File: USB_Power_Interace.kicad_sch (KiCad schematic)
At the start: 26 parts, among them CN1 USC_C_Receptacle_Hirose_CX90M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, SW1 SPST-NO, SW2 SPST-NO, U3 TPS2117DRL, U4 NCP167, U8 74HCT00

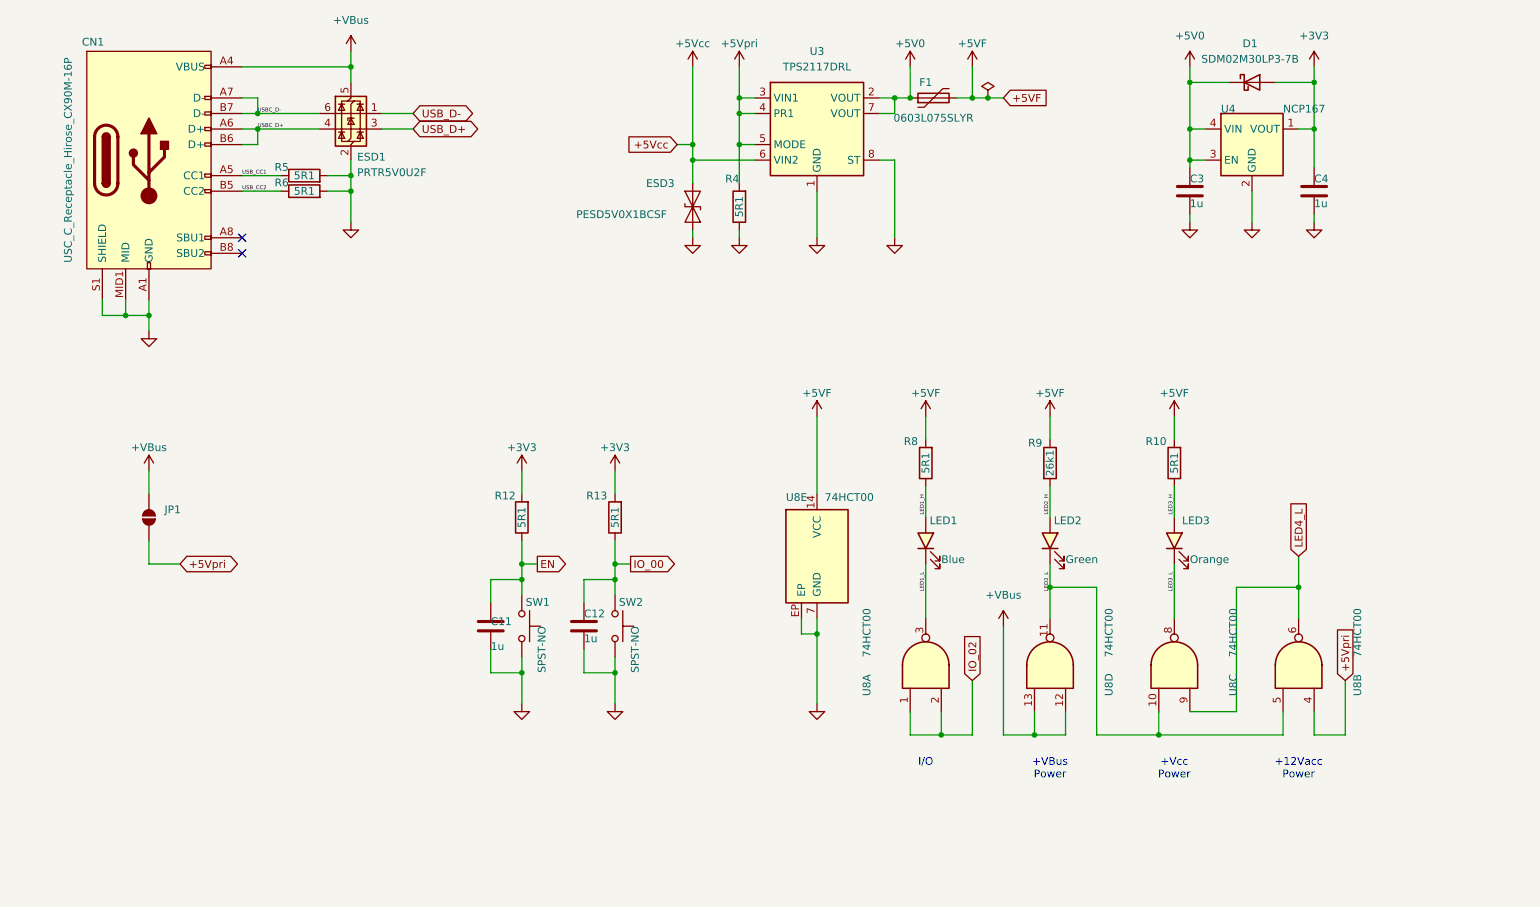
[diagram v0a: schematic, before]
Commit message: successful 1st pass, but I want to try some new bus'ing techniques to clean up the routing
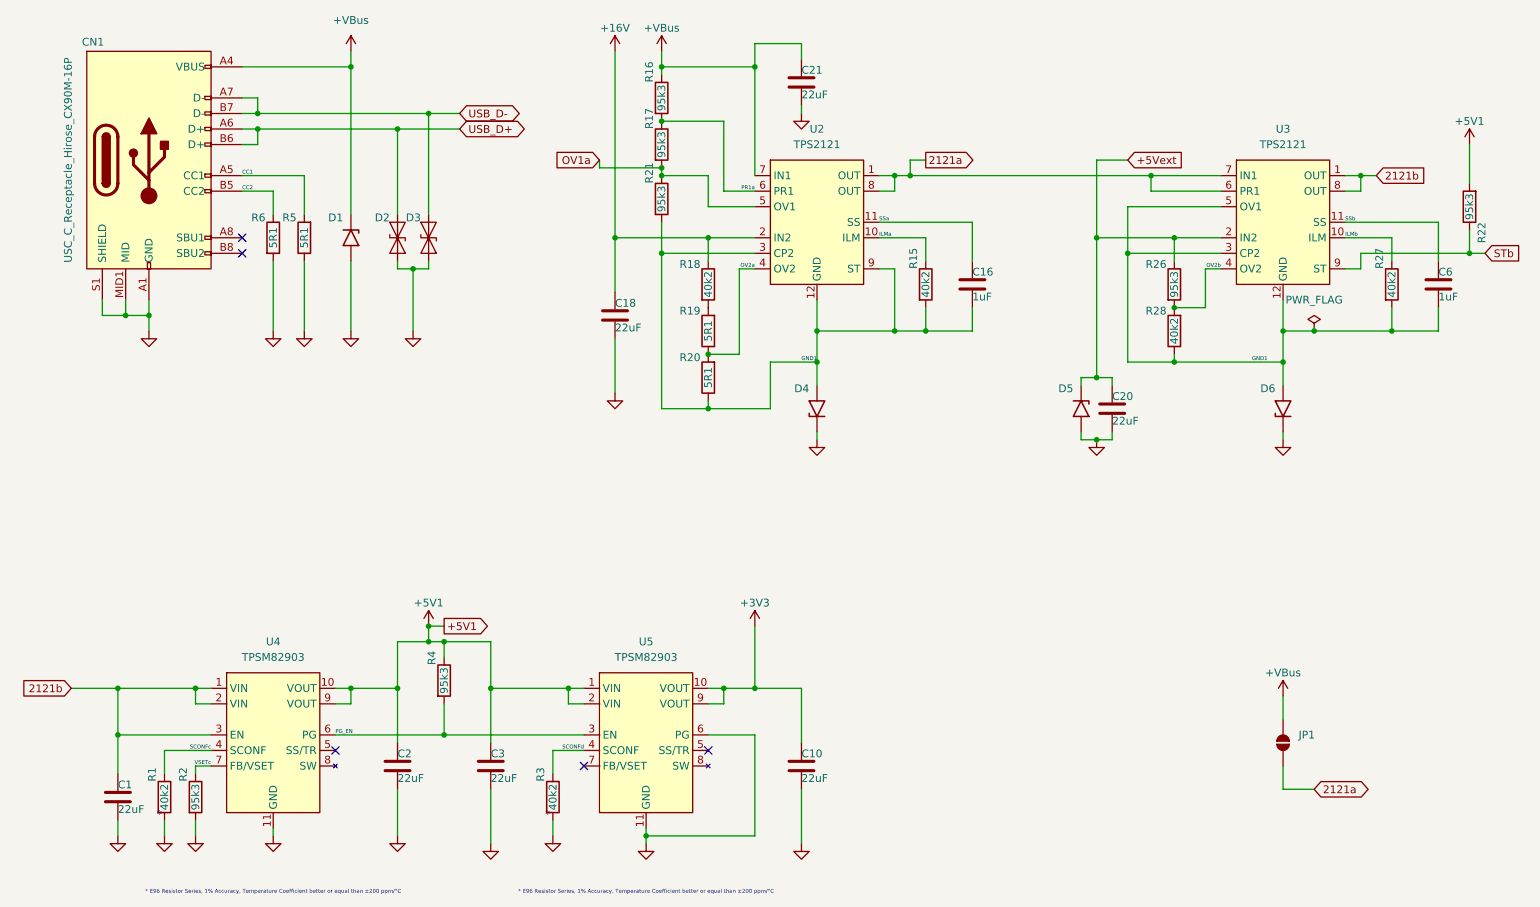
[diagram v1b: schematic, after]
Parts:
- removed C11, C12, C4: 1u, Capacitors:C0402_Nominal, symbol Device:C
- removed D1: SDM02M30LP3-7B, Personal_FootprintLibrary:DSN0603-2, symbol PersonalSchematicSymbolLibrary:SDM02M30LP3-7B
- removed ESD1: PRTR5V0U2F, Personal_FootprintLibrary:XSON6, symbol PersonalSchematicSymbolLibrary:PRTR5V0U2F
- removed ESD3: PESD5V0X1BCSF, Personal_FootprintLibrary:DSN0603-2, symbol PersonalSchematicSymbolLibrary:PESD5V0X1BCSF
- removed F1: 6V, 750mA, Personal_FootprintLibrary:Fuse_0603_1608Metric, symbol Device:Polyfuse
- removed LED1: Blue, Personal_FootprintLibrary:LED_0201-2, symbol PersonalSchematicSymbolLibrary:LED_Blue
- removed LED2: Green, Personal_FootprintLibrary:LED_0201-2, symbol PersonalSchematicSymbolLibrary:LED_Green
- removed LED3: Orange, Personal_FootprintLibrary:LED_0201-2, symbol PersonalSchematicSymbolLibrary:LED_Orange
- removed R10, R12, R13, R8: 5R1, Resistors:R0201_Nominal, symbol Device:R
- removed R9: 26k1, Resistors:R0201_Nominal, symbol Device:R
- removed SW1, SW2: SPST-NO, Personal_FootprintLibrary:SW_SPST_B3U_series, symbol PersonalSchematicSymbolLibrary:SW_Push_Button_NO
- removed U3: TPS2117DRL, Personal_FootprintLibrary:SOT5x3, symbol PersonalSchematicSymbolLibrary:TPS2117DRL
- removed U4: NCP167, Personal_FootprintLibrary:XDFN4_1.0x1.0mm, symbol PersonalSchematicSymbolLibrary:NCP167
- removed U8: 74HCT00, Personal_FootprintLibrary:WQFN-14-1EP_2.5x3mm_P0.5mm_EP1x1.5mm, symbol 74xx:74HCT00
- added C1, C18: 22uF, Capacitors:C0603_Dense, symbol Device:C
- added C10, C2: 22uF, Capacitors:C0402_Nominal, symbol Device:C
- added C16, C6: 1uF, Capacitors:C0201_Dense, symbol Device:C
- added C20, C21: 22uF, Capacitors:C0402_Dense, symbol Device:C
- added D1, D4, D5, D6: VESD16C1-HD1HG3-08, Personal_FootprintLibrary:DFN1006-2, symbol PersonalSchematicSymbolLibrary:TVS_Unidirectional
- added D2, D3: PESD24VF1BL-Q, Personal_FootprintLibrary:DFN1006-2, symbol PersonalSchematicSymbolLibrary:PESD24VF1BBL-Q
- added R1, R15, R18, R27, R28, R3: 40k2, Resistors:R0201_Dense, symbol Device:R
- added R16, R17, R2, R21, R22, R26: 95k3, Resistors:R0201_Dense, symbol Device:R
- added R19, R20: 5R1, Resistors:R0201_Dense, symbol Device:R
- added U2, U3: TPS2121, Personal_FootprintLibrary:VQHN-HR-12, symbol PersonalSchematicSymbolLibrary:TPS2121
- added U4, U5: TPSM82903, Personal_FootprintLibrary:uSIP-11_3.0x2.8_ThermalVias, symbol PersonalSchematicSymbolLibrary:TPSM82903
- C3: value 1u -> 22uF; Distributor Link 1 https://www.digikey.com/en/products/detail/samsung-electro-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 -> https://www.digikey.com/en/products/detail/murata-electroni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; Distributor Link 2 https://www.mouser.com/ProductDetail/Samsung-Electro-Mechan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 -> https://www.mouser.com/ProductDetail/Murata-Electronics/GRM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; LCSC C52923 -> C3845593; Manufacturer Samsung -> Murata Electronics; Manufacturer Part Number CL05A105KA5NQNC -> GRM158R61A226ME15D
- R4: value 5R1 -> 95k3; footprint Resistors:R0201_Nominal -> Resistors:R0201_Dense; Distributor Link 2 https://www.mouser.com/ProductDetail/Royalohm/PF01WMF5100TE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 -> https://www.mouser.com/ProductDetail/Royalohm/0201WMF9532TE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; LCSC C50670526 -> C423395; Manufacturer Part Number PF01WMF510KTEE -> 0201WMF9532TEE
- R5, R6: footprint Resistors:R0201_Nominal -> Resistors:R0201_Dense
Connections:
- net USBC_D+ is gone; now on net USB_D+: CN1.A6 (D+), CN1.B6 (D+)
- net USBC_D- is gone; now on net USB_D-: CN1.A7 (D-), CN1.B7 (D-)
- net +3V3: now also C10.1, U5.10 (VOUT), U5.9 (VOUT)
- net +VBus: now also C21.1, D1.1 (A1), R16.1, U2.7 (IN1)
- net GND: now also R5.1, C1.2, C10.2, C18.2, C2.2, C20.2, C21.2, D1.2 (A2), D2.1 (A1), D3.1 (A1), D4.1 (A1), D5.2 (A2), D6.1 (A1), R1.2, R2.2, R3.2, U4.11 (GND), U5.11 (GND), U5.6 (PG); no longer R4.1, R5.2
- net USB_D+: now also D2.2 (A2)
- net USB_D-: now also D3.2 (A2)
- net +5V0 renamed +5V1
- net +5V1: now also R4.1, C2.1, R22.2, U4.10 (VOUT), U4.9 (VOUT), U5.1 (VIN), U5.2 (VIN)
- net +5Vpri renamed 2121a
- net 2121a: now also U2.1 (OUT), U2.8 (OUT), U3.6 (PR1), U3.7 (IN1); no longer R4.2
- net USB_CC1 renamed CC1
- net CC1: now also R5.2; no longer R5.1
- net USB_CC2 renamed CC2
- new net: R18.2, R19.2
- new net +16V: C18.1, R18.1, U2.2 (IN2)
- new net +5Vext: C20.1, D5.1 (A1), R26.1, U3.2 (IN2)
- new net 2121b: C1.1, U3.1 (OUT), U3.8 (OUT), U4.1 (VIN), U4.2 (VIN), U4.3 (EN)
- new net GND1: C16.2, C6.2, D4.2 (A2), D6.2 (A2), R15.2, R20.1, R21.2, R27.2, R28.1, U2.12 (GND), U2.3 (CP2), U2.9 (ST), U3.12 (GND), U3.3 (CP2), U3.5 (OV1)
- new net ILMa: R15.1, U2.10 (ILM)
- new net ILMb: R27.1, U3.10 (ILM)
- new net OV1a: R17.2, R21.1, U2.5 (OV1)
- new net OV2a: R19.1, R20.2, U2.4 (OV2)
- new net OV2b: R26.2, R28.2, U3.4 (OV2)
- new net PG_EN: R4.2, U4.6 (PG), U5.3 (EN)
- new net PR1a: R16.2, R17.1, U2.6 (PR1)
- new net SCONFc: R1.1, U4.4 (SCONF)
- new net SCONFd: R3.1, U5.4 (SCONF)
- new net SSa: C16.1, U2.11 (SS)
- new net SSb: C6.1, U3.11 (SS)
- new net STb: R22.1, U3.9 (ST)
- new net VSETc: R2.1, U4.7 (FB/VSET)
- no-connect marks 2 -> 5
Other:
- note added: "*"
- note added: "* E96 Resistor Series, 1% Accuracy, Temperature Coefficient better or equal than ±200 ppm/°C"
- note removed: "+12Vacc Power"
- note removed: "+VBus Power"
- note removed: "+Vcc Power"
- note removed: "I/O"
- moved on the sheet: JP1, R5, R6

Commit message: Update CAN_Interface.kicad_sch, ESP32-S3 Pico D1.kicad_dru, ESP32-S3 Pico D1.kicad_pcb, and 5 more files reroute completed
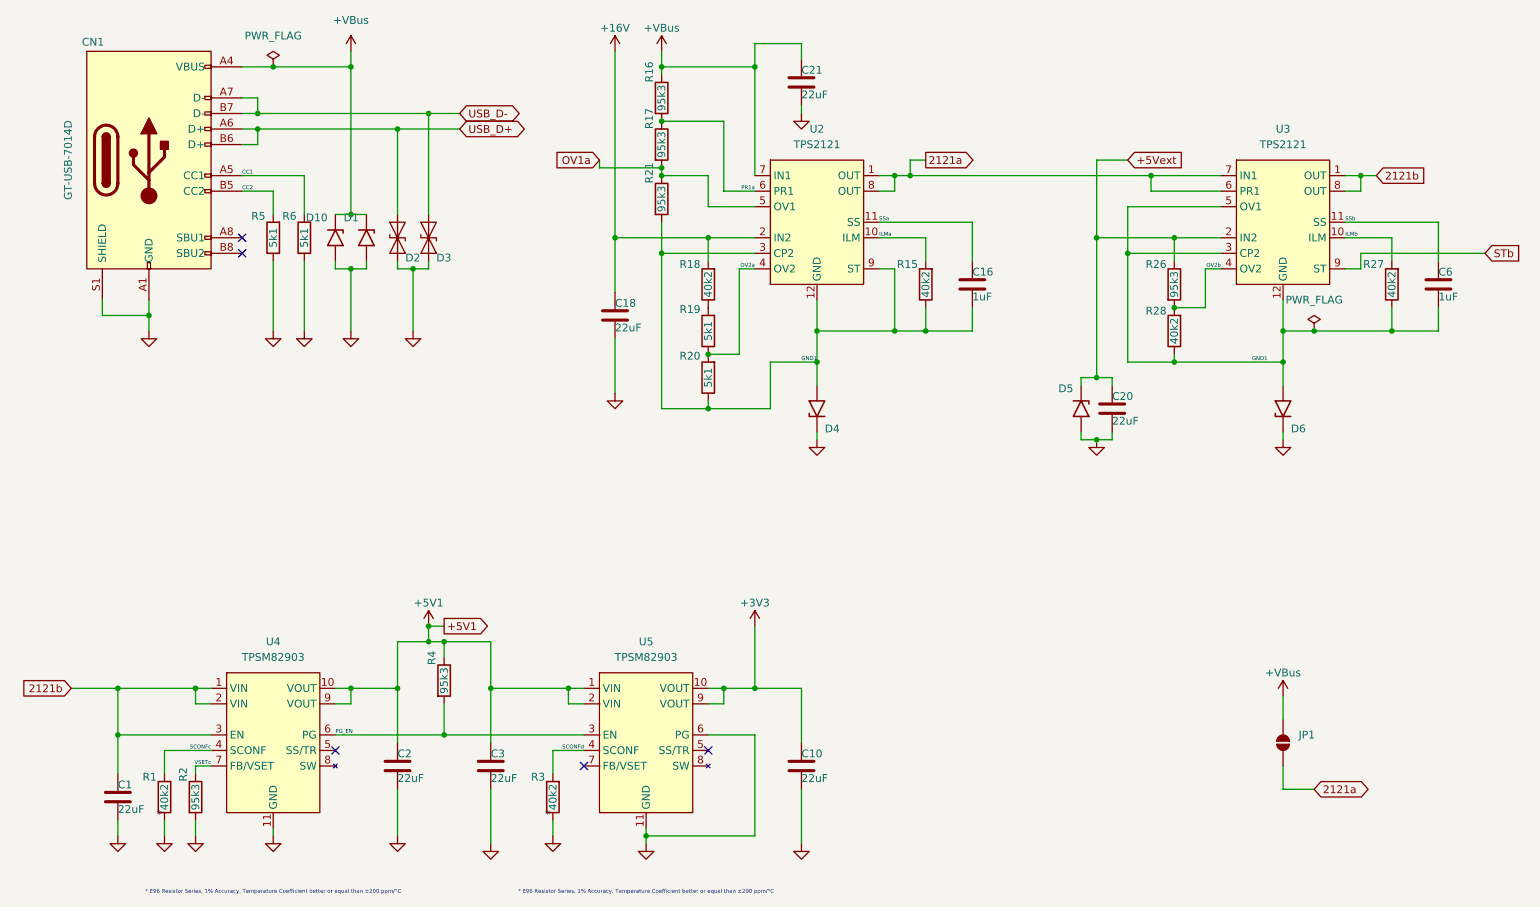
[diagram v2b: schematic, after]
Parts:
- removed R22: 95k3, Resistors:R0201_Dense, symbol Device:R
- added D10: D15V0H1U2LP-7B, Personal_FootprintLibrary:DFN1006-2, symbol PersonalSchematicSymbolLibrary:TVS_Unidirectional
- C10, C2, C3: footprint Capacitors:C0402_Nominal -> Capacitors:C0402_Dense
- CN1: value USC_C_Receptacle_Hirose_CX90M-16P -> GT-USB-7014D; footprint Personal_FootprintLibrary:USB_C_Receptacle_Hirose_CX90M-16P -> Personal_FootprintLibrary:USB_C_Receptacle_G-Switch-GT-USB-7014D; Distributor Link 1 https://www.digikey.com/en/products/detail/hirose-electric-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 -> (none); Distributor Link 2 https://www.mouser.com/ProductDetail/Hirose-Connector/CX90M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 -> (none); LCSC C2889324 -> C2843969; Manufacturer Hirose -> G-Switch; Manufacturer Part Number CX90M-16P -> GT-USB-7014D
- D1, D4, D5, D6: value VESD16C1-HD1HG3-08 -> D15V0H1U2LP-7B; Distributor Link 1 https://www.digikey.com/en/products/detail/vishay-general-s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 -> https://www.digikey.com/en/products/detail/diodes-incorpora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; Distributor Link 2 https://www.mouser.com/ProductDetail/Vishay-General-Semicon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 -> https://www.mouser.com/ProductDetail/Diodes-Incorporated/D1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; LCSC C3703781 -> C1973850; Manufacturer Vishay -> Diodes Incorporated; Manufacturer Part Number VESD16C1-HD1HG3-08 -> D15V0H1U2LP-7B
- D2, D3: value PESD24VF1BL-Q -> ESDSLC24VLB-TP; Distributor Link 1 https://www.digikey.com/en/products/detail/nexperia-usa-inc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 -> https://www.digikey.com/en/products/detail/mcc-micro-commer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; Distributor Link 2 https://www.mouser.com/ProductDetail/Nexperia/PESD24VF1BBL-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 -> https://www.mouser.com/ProductDetail/Micro-Commercial-Compo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; LCSC C22465859 -> C7463931; Manufacturer Nexperia -> MCC(Micro Commercial Components); Manufacturer Part Number PESD24VF1BBL-Q -> ESDSLC24VLB-TP
- R1, R3: Distributor Link 1 https://www.digikey.com/en/products/detail/yageo/AC0201FR-0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 -> (none); Distributor Link 2 https://www.mouser.com/ProductDetail/YAGEO/AC0201FR-0726K1L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 -> https://www.mouser.com/ProductDetail/Royalohm/0201WMF4022TE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; LCSC C910625 -> C423536; Manufacturer Yageo -> UNI-ROYAL(Uniroyal Elec); Manufacturer Part Number AC0201FR-0726K1L -> 0201WMF4022TEE
- R15, R18, R27: Distributor Link 2 https://www.mouser.com/ProductDetail/Royalohm/0201WMF9532TE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 -> https://www.mouser.com/ProductDetail/Royalohm/0201WMF4022TE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; LCSC C423395 -> C423536; Manufacturer Part Number 0201WMF9532TEE -> 0201WMF4022TEE
- R19, R20, R5, R6: value 5R1 -> 5k1; Distributor Link 2 https://www.mouser.com/ProductDetail/Royalohm/PF01WMF5100TE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 -> https://www.mouser.com/ProductDetail/Royalohm/0201WMF5101TE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; LCSC C50670526 -> C270344; Manufacturer Part Number PF01WMF510KTEE -> 0201WMF5101TEE
- R28: Distributor Link 2 https://www.mouser.com/ProductDetail/Royalohm/PF01WMF5100TE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 -> https://www.mouser.com/ProductDetail/Royalohm/0201WMF4022TE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; LCSC C50670526 -> C423536; Manufacturer Part Number PF01WMF510KTEE -> 0201WMF4022TEE
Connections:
- net +16V: now also R18.2; no longer R18.1
- net +VBus: now also D10.1 (A1)
- net CC1: now also R6.2; no longer R5.2
- net CC2: now also R5.2; no longer R6.1
- net GND: now also D2.2 (A2), D3.2 (A2), R1.1, R3.1, R6.1, D10.2 (A2); no longer CN1.MID1 (MID), CN1.MID2 (MID), D2.1 (A1), D3.1 (A1), R1.2, R3.2, R6.2
- net GND1: now also R15.1, R27.1; no longer R15.2, R27.2
- net ILMa: now also R15.2; no longer R15.1
- net ILMb: now also R27.2; no longer R27.1
- net SCONFc: now also R1.2; no longer R1.1
- net SCONFd: now also R3.2; no longer R3.1
- net USB_D+: now also D2.1 (A1); no longer D2.2 (A2)
- net USB_D-: now also D3.1 (A1); no longer D3.2 (A2)
- net at R19.2: now also R18.1; no longer R18.2
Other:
- moved on the sheet: D2
